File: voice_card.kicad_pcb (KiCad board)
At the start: 2 copper layers, 119.3 x 38 mm, 209 parts, among them J1 PCI_11_49, Q1 MMBF4391LT1G, Q10 DMMT3906, Q11 BC857BS, Q2 2N3904, Q3 BCM847, Q4 DMMT3904, Q5 DMMT3906, Q6 MMBF4391LT1G, Q7 BCM847, Q8 2N3904, Q9 DMMT3904, U1 TL074-, U10 TL072-, U11 TL074-, U12 NE555, U13 LM311M, U14 CD4052, U15 TL072-, U16 TL072-, U17 LM13700, U18 LM13700, U19 LM13700, U2 TL074-, U20 TL072-, U3 NE555, U4 LF351, U5 TL072-, U6 LM311M, U7 CD4052, U8 TL074-, U9 LF351

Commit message: still working on vcf/vca. getting there
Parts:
- moved R28 5.62 mm to (84.2, 70.2), turned to 180 degrees
- moved R67 5.49 mm to (110.5, 70.2), turned to 180 degrees
- moved R58 3.04 mm to (127.2, 83.2), turned to 0 degrees
- moved R16 2.94 mm to (100.5, 83.2), turned to 0 degrees
- moved R98 2.66 mm to (134.2, 65.8)
- moved R103 1.77 mm to (134.2, 69.2)
- moved R105 1.77 mm to (134.2, 71.0)
- moved R27 1.77 mm to (82.5, 68.5)
- moved R66 1.60 mm to (108.8, 68.5)
- moved R60 0.56 mm to (110.5, 66.8)
- moved R18 0.50 mm to (84.2, 66.8)
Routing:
- net VCO2_SAW: track 16.1 -> 27.8 mm
- net -12V: track 34.4 -> 46.1 mm
- net VCA_IN: track 0.00 -> 6.62 mm
- net Net-(R103-Pad2): track 20.9 -> 27.4 mm
- net Net-(C33-Pad1): track 14.5 -> 17.8 mm
- net Net-(R105-Pad2): track 8.16 -> 4.87 mm
- net +12V: track 18.7 -> 21.9 mm, vias 6 -> 9
- net Net-(R53-Pad1): track 14.7 -> 12.3 mm
- net Net-(R18-Pad2): track 14.3 -> 12.1 mm
- net VCF_CTRL: track 0.00 -> 1.92 mm
- net VCO1_SYNC_IN: track 17.6 -> 16.1 mm
- net VCO2_TRI_SHAPE: track 19.5 -> 18.1 mm
- net VCO2_PITCH_CV: track 9.43 -> 8.12 mm
- net VCO1_PITCH_CV: track 10.5 -> 9.37 mm
- net VCF_IN: track 17.0 -> 15.9 mm
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
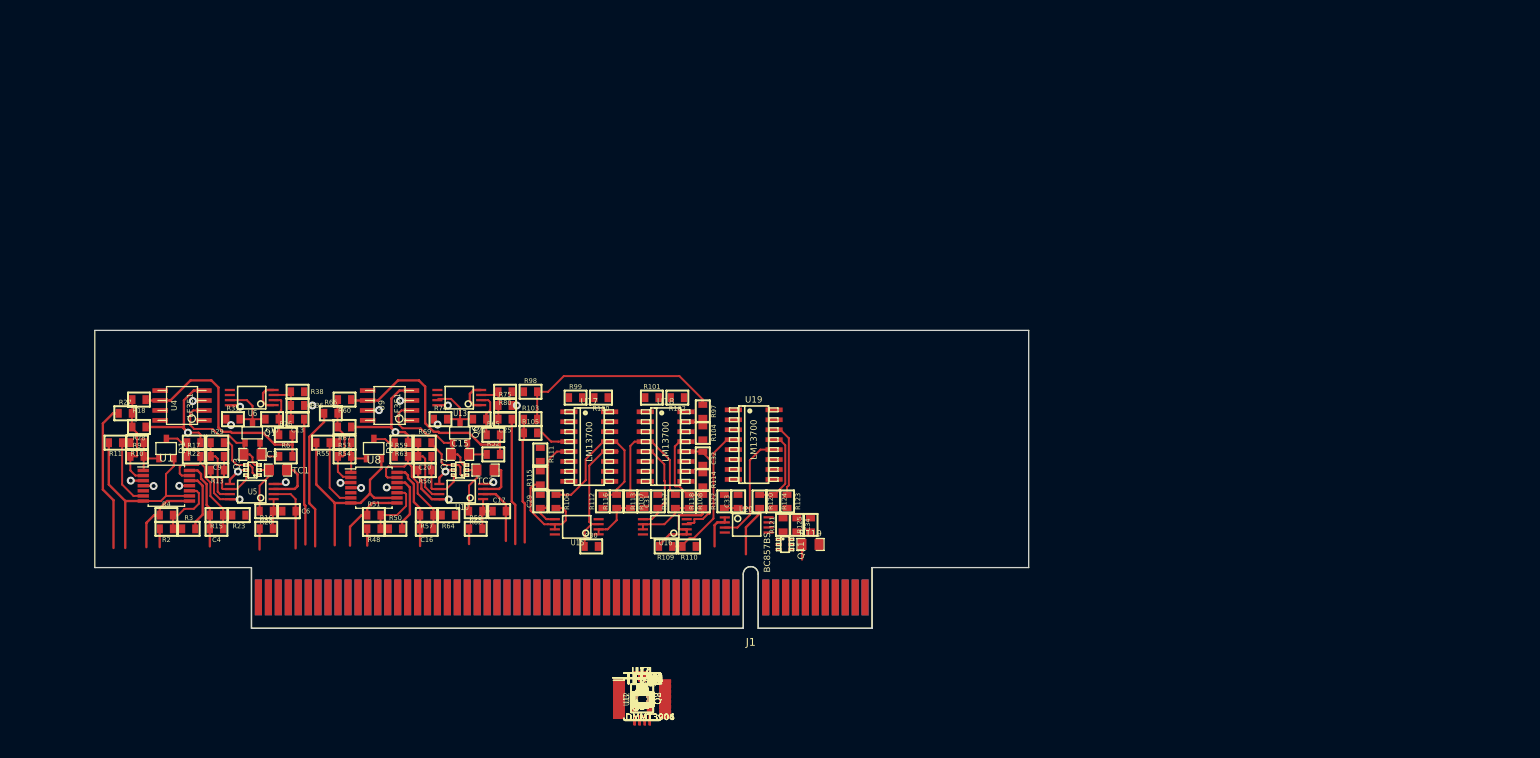
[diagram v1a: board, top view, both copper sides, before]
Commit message: struggling with EG component layout and routing. Thinking of replacing U2 (TL074) with two TL072s for ease of compact layout
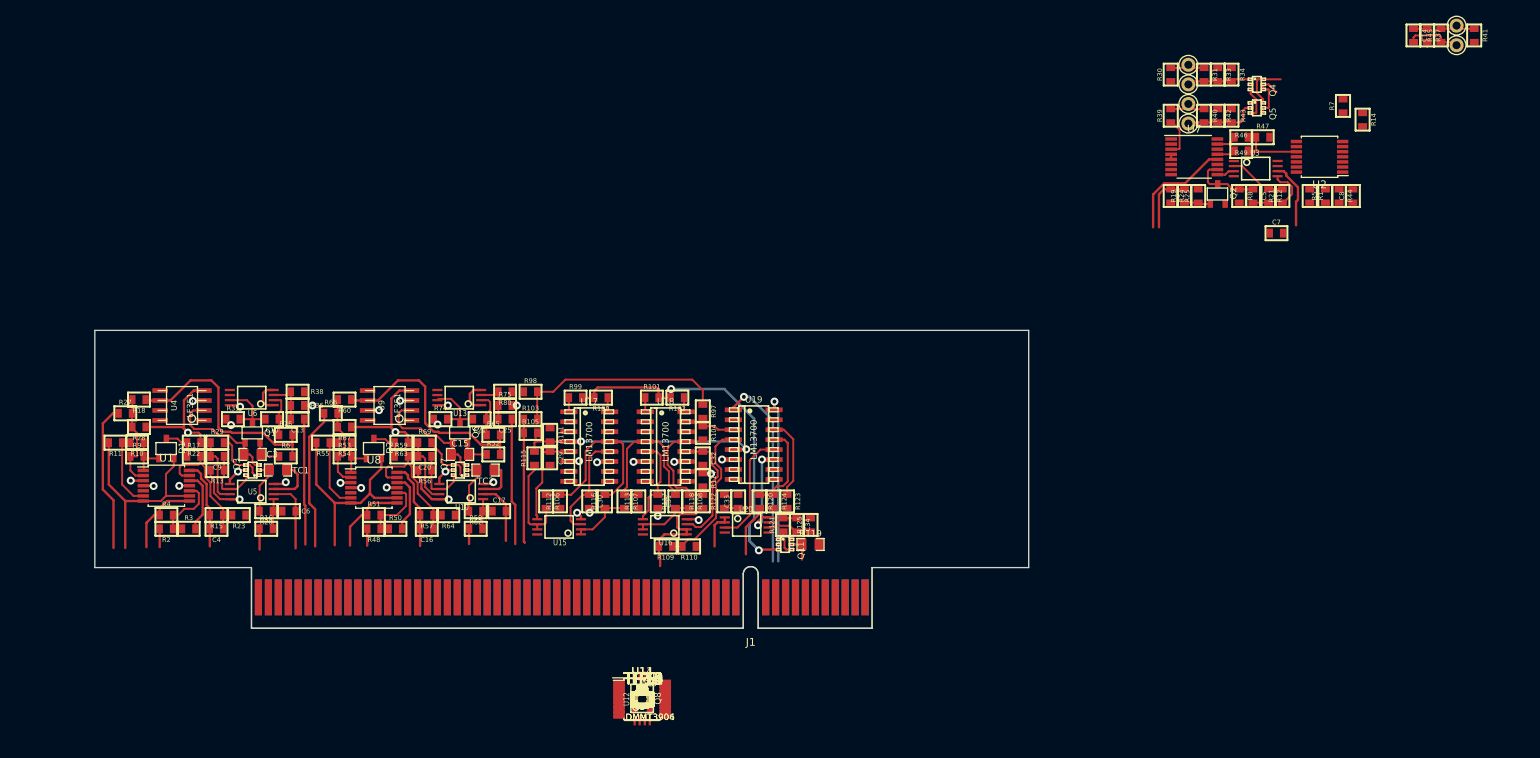
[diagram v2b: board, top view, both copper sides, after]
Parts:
- removed R32, R83: 1K, MyModules:SM0603-R-JRL
- moved R41 135.9 mm to (254.8, 20.2), turned to 270 degrees
- moved TP7 135.0 mm to (252.5, 19.0)
- moved TP6 133.4 mm to (252.5, 21.5)
- moved R45 132.6 mm to (250.5, 20.2), turned to 90 degrees
- moved R37 131.3 mm to (248.8, 20.2), turned to 270 degrees
- moved C14 129.9 mm to (247.0, 20.2), turned to 270 degrees
- moved R14 118.1 mm to (240.5, 31.0), turned to 270 degrees
- moved R7 117.3 mm to (238.0, 29.2), turned to 90 degrees
- moved C8 111.2 mm to (239.2, 40.8), turned to 90 degrees
- moved Q4 111.0 mm to (227.0, 26.5), turned to 270 degrees
- moved U2 110.8 mm to (235.0, 35.8), turned to 180 degrees
- moved R44 109.8 mm to (237.5, 40.8), turned to 270 degrees
- moved R34 109.6 mm to (223.8, 25.2), turned to 270 degrees
- moved Q5 108.9 mm to (227.0, 29.5), turned to 270 degrees
- moved R33 108.5 mm to (222.0, 25.2), turned to 270 degrees
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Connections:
- C27 pad 1: Net-(C27-Pad1) -> EG2_ENV_OUT
- C8 pad 1: Net-(C8-Pad1) -> EG1_ENV_OUT
- Q5 pad 1: Net-(Q5-Pad1) -> GND
- Q5 pad 2: GND -> Net-(Q5-Pad2)
- Q5 pad 3: Net-(C14-Pad2) -> Net-(C8-Pad2)
- Q5 pad 6: Net-(C8-Pad2) -> Net-(C14-Pad2)
- R40 pad 2: Net-(Q5-Pad1) -> Net-(Q5-Pad2)
- R42 pad 2: Net-(Q5-Pad1) -> Net-(Q5-Pad2)
- R43 pad 2: Net-(Q5-Pad1) -> Net-(Q5-Pad2)
- R44 pad 2: Net-(C8-Pad1) -> EG1_ENV_OUT
- R5 pad 1: Net-(C8-Pad1) -> EG1_ENV_OUT
- R68 pad 1: Net-(C27-Pad1) -> EG2_ENV_OUT
- R92 pad 2: Net-(C27-Pad1) -> EG2_ENV_OUT
- TP5 pad 1: Net-(Q5-Pad1) -> Net-(Q5-Pad2)
- U11 pad 7: Net-(C27-Pad1) -> EG2_ENV_OUT
- U12 pad 6: Net-(C27-Pad1) -> EG2_ENV_OUT
- U2 pad 1: EG1_INV_OUT -> Net-(C14-Pad1)
- U2 pad 10: GND -> Net-(R47-Pad1)
- U2 pad 12: Net-(R47-Pad1) -> Net-(R14-Pad2)
- U2 pad 13: Net-(R41-Pad2) -> Net-(R1-Pad1)
- U2 pad 14: Net-(R41-Pad1) -> EG1_INV_OUT
- U2 pad 2: Net-(R1-Pad1) -> Net-(C14-Pad2)
- U2 pad 3: Net-(R14-Pad2) -> GND
- U2 pad 7: Net-(C8-Pad1) -> EG1_ENV_OUT
- U2 pad 8: Net-(C14-Pad1) -> Net-(R41-Pad1)
- U2 pad 9: Net-(C14-Pad2) -> Net-(R41-Pad2)
- U3 pad 6: Net-(C8-Pad1) -> EG1_ENV_OUT
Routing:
- net Iabc: track 0.00 -> 46.9 mm, vias 0 -> 2
- net Net-(R105-Pad2): track 4.87 -> 31.9 mm, vias 0 -> 2
- net RES_CTRL: track 0.00 -> 25.2 mm, vias 0 -> 1
- net VCA_CTRL: track 0.00 -> 22.5 mm, vias 0 -> 1
- net +12V: track 21.9 -> 39.0 mm, vias 9 -> 13
- net EG1_SUSTAIN_CV: track 0.00 -> 14.3 mm
- net Net-(C14-Pad2): track 0.00 -> 13.8 mm
- net Net-(Q5-Pad2): track 0.00 -> 9.48 mm
- net Net-(C5-Pad1): track 0.00 -> 8.83 mm
- net Net-(C5-Pad2): track 0.00 -> 8.71 mm
- net EG1_ENV_OUT: track 0.00 -> 8.57 mm
- net Net-(Q4-Pad1): track 0.00 -> 8.22 mm
- net Net-(R47-Pad1): track 0.00 -> 8.13 mm
- net Net-(Q4-Pad4): track 0.00 -> 7.78 mm
- net EG1_GATE: track 0.00 -> 7.74 mm
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
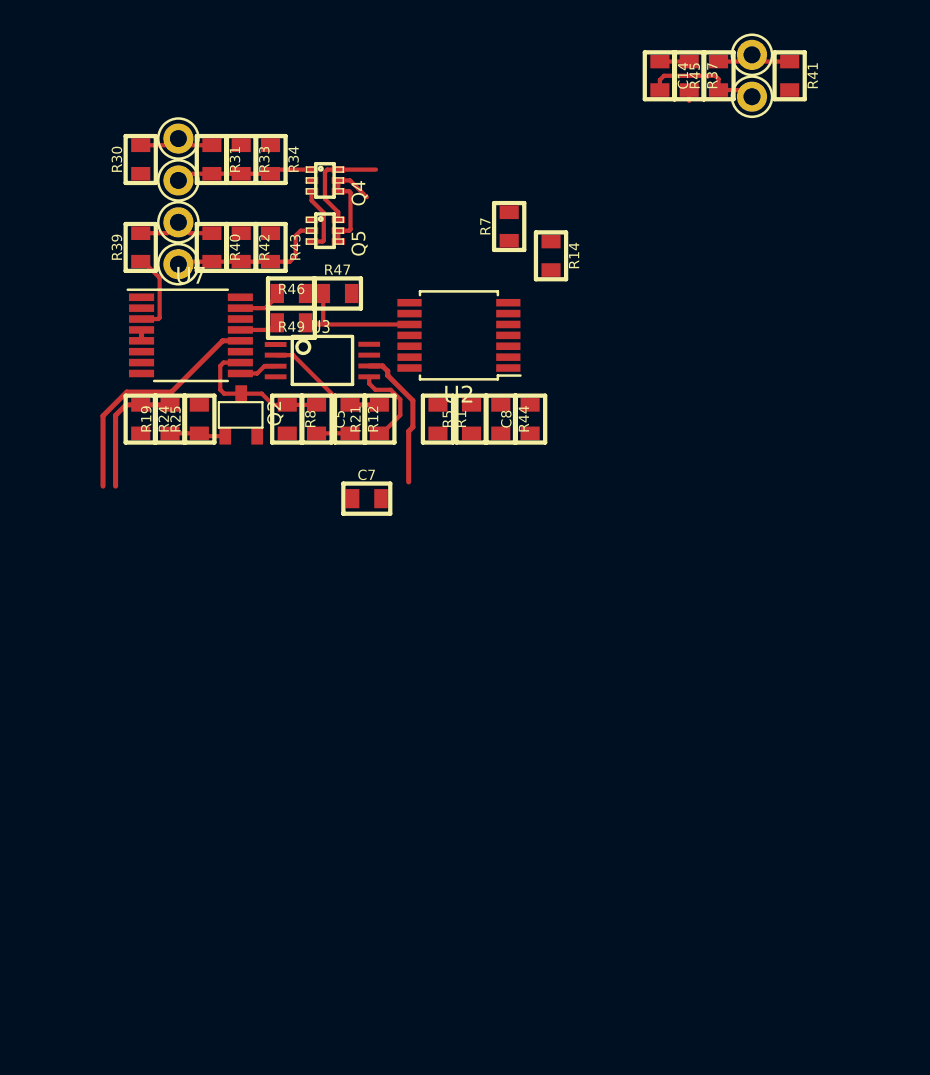
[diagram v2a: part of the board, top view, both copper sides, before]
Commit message: EG1 routed, just flipping and fitting now
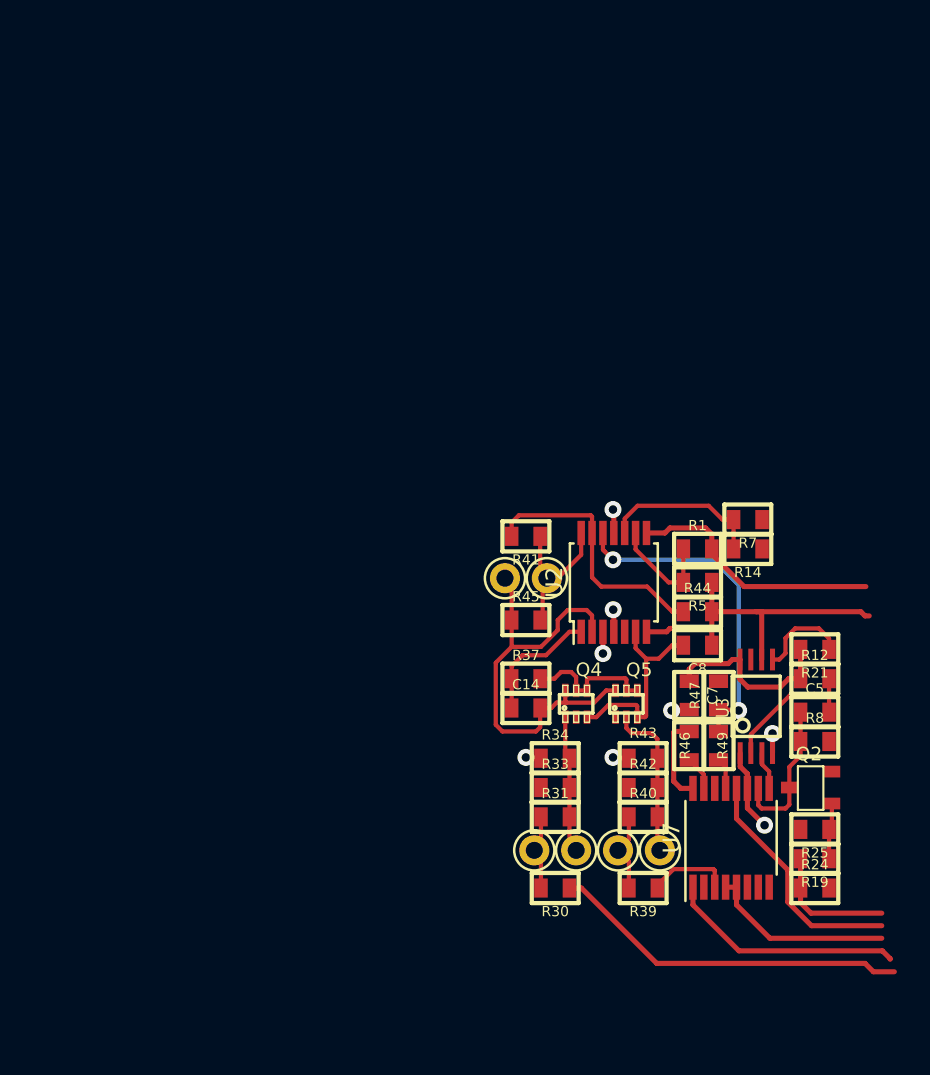
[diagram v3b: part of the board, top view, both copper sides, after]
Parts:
- moved R30 50.0 mm to (240.8, 68.8), turned to 180 degrees
- moved R24 49.0 mm to (256.2, 68.8), turned to 0 degrees
- moved R39 48.6 mm to (246.0, 68.8), turned to 180 degrees
- moved TP2 47.5 mm to (239.5, 66.5), turned to 90 degrees
- moved R19 46.6 mm to (256.2, 67.0), turned to 180 degrees
- moved TP3 46.5 mm to (242.0, 66.5), turned to 90 degrees
- moved TP4 45.8 mm to (244.5, 66.5), turned to 90 degrees
- moved TP5 45.3 mm to (247.0, 66.5), turned to 90 degrees
- moved R31 44.3 mm to (240.8, 64.5), turned to 0 degrees
- moved R25 44.2 mm to (256.2, 65.2), turned to 180 degrees
- moved U7 44.0 mm to (251.2, 65.8), turned to 90 degrees
- moved R40 42.7 mm to (246.0, 64.5), turned to 0 degrees
- moved R33 41.9 mm to (240.8, 62.8), turned to 0 degrees
- moved Q2 40.6 mm to (256.0, 62.8), turned to 90 degrees
- moved R42 40.2 mm to (246.0, 62.8), turned to 0 degrees
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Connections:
- U2 pad 10: Net-(R47-Pad1) -> Net-(R14-Pad2)
- U2 pad 12: Net-(R14-Pad2) -> Net-(R47-Pad1)
- U2 pad 13: Net-(R1-Pad1) -> Net-(R41-Pad2)
- U2 pad 14: EG1_INV_OUT -> Net-(R41-Pad1)
- U2 pad 8: Net-(R41-Pad1) -> EG1_INV_OUT
- U2 pad 9: Net-(R41-Pad2) -> Net-(R1-Pad1)
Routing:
- net EG1_ATTACK_CV: track 0.00 -> 21.5 mm
- net +12V: track 39.0 -> 55.9 mm, vias 13 -> 15
- net Net-(R41-Pad2): track 0.00 -> 15.9 mm
- net EG1_INV_OUT: track 0.00 -> 15.4 mm
- net EG1_DECAY_CV: track 0.00 -> 14.2 mm
- net Net-(C14-Pad2): track 13.8 -> 27.7 mm
- net Net-(R47-Pad1): track 8.13 -> 20.0 mm, vias 0 -> 2
- net EG1_ENV_OUT: track 8.57 -> 20.4 mm
- net EG1_RELEASE_CV: track 0.65 -> 11.2 mm
- net Net-(R14-Pad2): track 0.00 -> 9.77 mm
- net Net-(C8-Pad2): track 3.99 -> 12.4 mm
- net GND: track 45.1 -> 52.4 mm, vias 11 -> 14
- net Net-(R1-Pad1): track 0.00 -> 6.64 mm
- net Net-(C14-Pad1): track 1.75 -> 7.50 mm
- net Net-(R41-Pad1): track 4.58 -> 9.74 mm
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
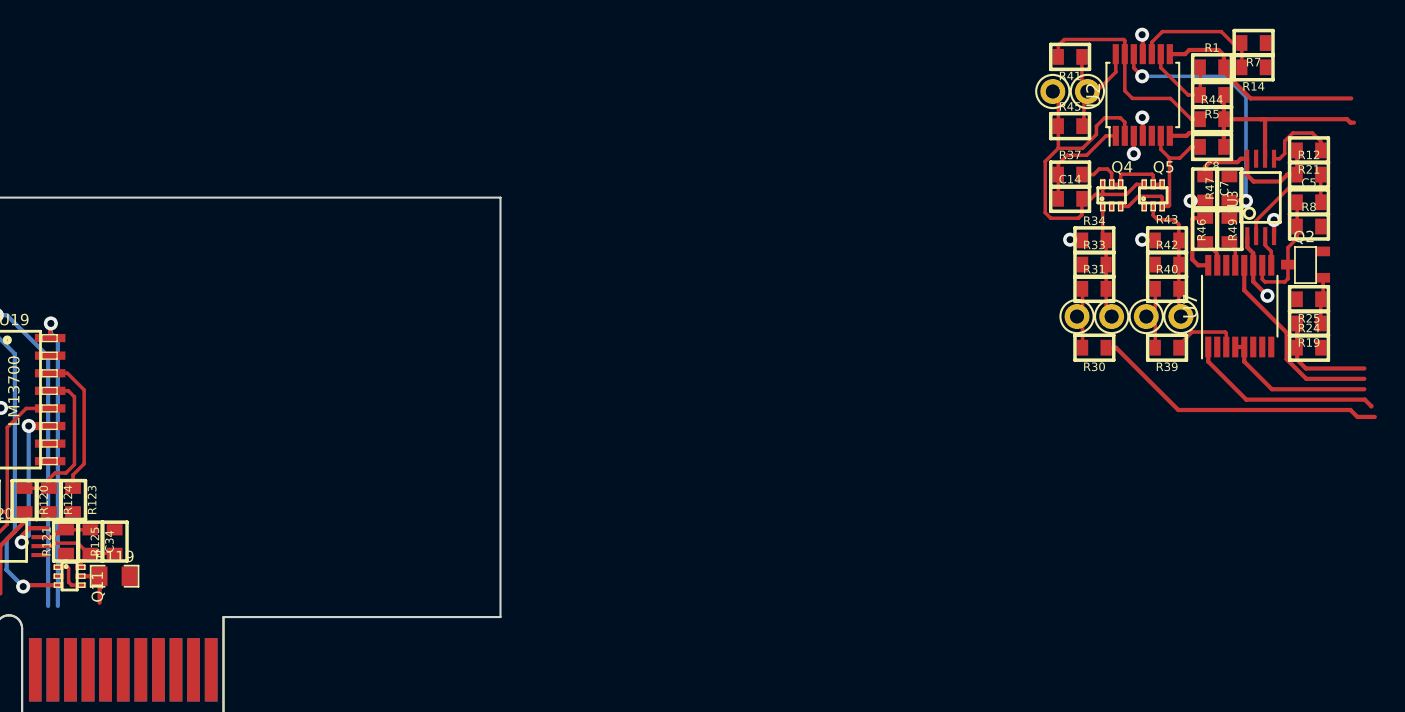
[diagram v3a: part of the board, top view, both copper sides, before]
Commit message: EG1 routed, some adjustments made to increase compactness
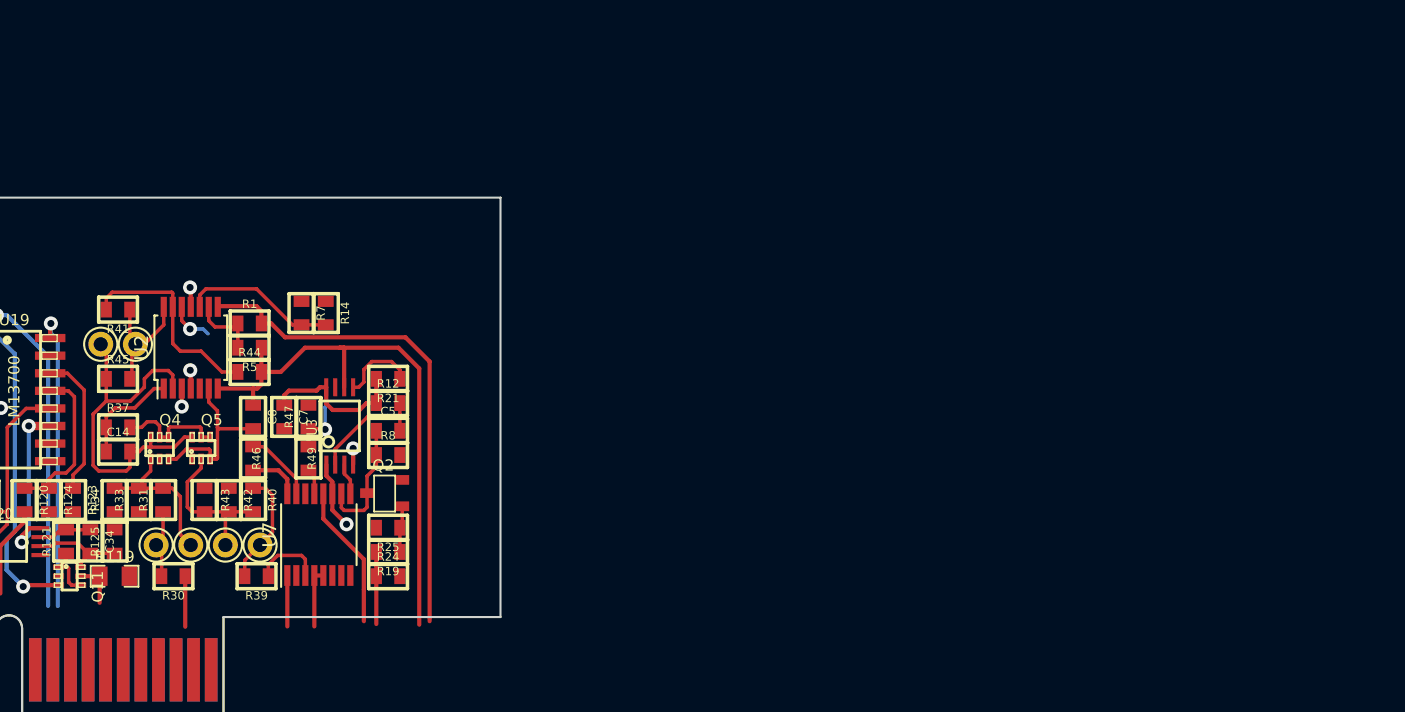
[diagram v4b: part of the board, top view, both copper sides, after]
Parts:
- moved R34 73.2 mm to (170.0, 79.8), turned to 90 degrees
- moved R43 72.0 mm to (176.5, 79.8), turned to 270 degrees
- moved C8 71.9 mm to (180.0, 73.8), turned to 270 degrees
- moved R1 71.9 mm to (179.8, 67.0)
- moved R44 71.9 mm to (179.8, 70.5)
- moved R5 71.9 mm to (179.8, 68.8)
- moved R7 71.5 mm to (183.5, 66.2), turned to 270 degrees
- moved C14 71.1 mm to (170.2, 76.2)
- moved Q4 71.1 mm to (173.2, 76.0)
- moved Q5 71.1 mm to (176.2, 76.0)
- moved R37 71.1 mm to (170.2, 74.5)
- moved R41 71.1 mm to (170.2, 66.0)
- moved R45 71.1 mm to (170.2, 71.0)
- moved TP6 71.1 mm to (169.0, 68.5)
- moved TP7 71.1 mm to (171.5, 68.5)
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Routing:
- net EG1_ENV_OUT: track 20.4 -> 41.6 mm
- net EG1_INV_OUT: track 15.4 -> 36.3 mm
- net EG1_ATTACK_CV: track 21.5 -> 3.65 mm
- net Net-(R47-Pad1): track 20.0 -> 7.53 mm
- net EG1_DECAY_CV: track 14.2 -> 3.67 mm
- net EG1_RELEASE_CV: track 11.2 -> 4.32 mm
- net EG1_SUSTAIN_CV: track 14.3 -> 10.4 mm
- net Net-(R39-Pad2): track 4.79 -> 8.50 mm
- net Net-(Q4-Pad1): track 8.22 -> 11.8 mm
- net Net-(R46-Pad2): track 2.06 -> 5.18 mm
- net EG1_GATE: track 7.74 -> 5.20 mm
- net -12V: track 56.3 -> 54.4 mm, vias 14 -> 12
- net Net-(Q5-Pad2): track 9.48 -> 11.3 mm
- net Net-(R1-Pad1): track 6.64 -> 5.14 mm
- net Net-(R14-Pad2): track 9.77 -> 11.2 mm
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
